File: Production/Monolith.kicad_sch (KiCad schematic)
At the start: 0 parts

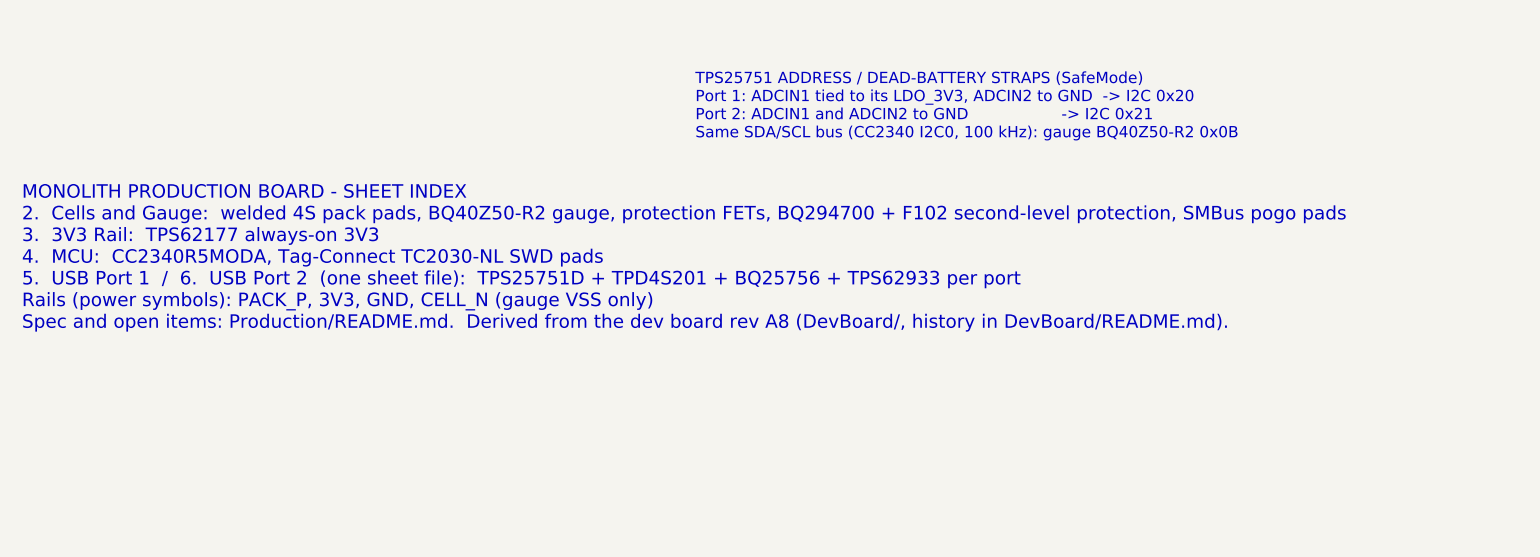
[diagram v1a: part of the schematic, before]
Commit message: Production schematic P0: U405/U505 TPD4S201 -> TPD2S300 (CC only)
CC keeps short-to-VBUS OVP and IEC ESD (TPS25751 CC pins are only +-1 kV
HBM); SBU half dropped with liquid detection, connector SBU pins no-connect.
VPWR/VM on LDO_3V3, VBIAS C451, FLT -> GPIO3. tools/tpd2s300.py. Netlist check
passes; ERC unchanged. Courtyard 1923 -> 1884 mm2.

Co-Authored-By: Claude Opus 5.5 <noreply@anthropic.com>
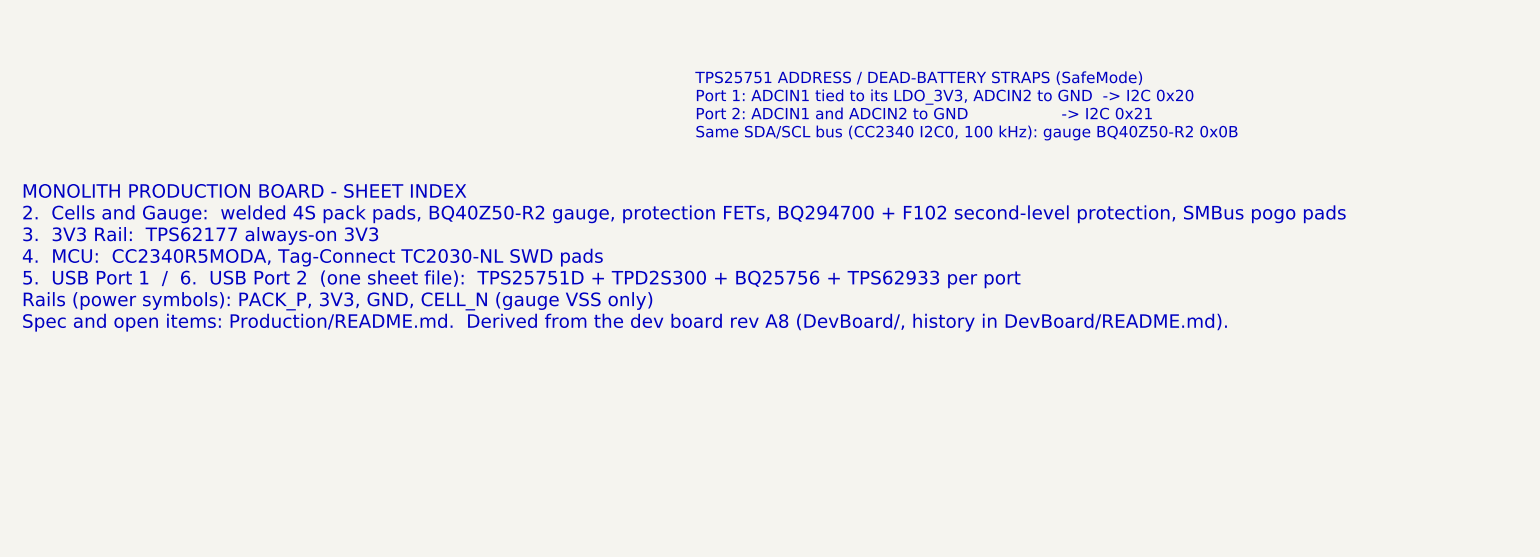
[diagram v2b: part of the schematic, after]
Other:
- note added: "MONOLITH PRODUCTION BOARD - SHEET INDEX 2. Cells and Gauge: welded 4S pack pads, BQ40Z50-R2 gauge, protection FETs, BQ294700 + F102 second-level protection, SMBus pogo pads 3. 3V3 Rail: TPS62177 always-on 3V3 4. MCU: CC2340R5MODA, Tag-Connect TC2030-NL SWD pads 5. USB Port 1 / 6. USB Port 2 (one sheet file): TPS25751D + TPD2S300 + BQ25756 + TPS62933 per port Rails (power symbols): PACK_P, 3V3, GN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"
- note removed: "MONOLITH PRODUCTION BOARD - SHEET INDEX 2. Cells and Gauge: welded 4S pack pads, BQ40Z50-R2 gauge, protection FETs, BQ294700 + F102 second-level protection, SMBus pogo pads 3. 3V3 Rail: TPS62177 always-on 3V3 4. MCU: CC2340R5MODA, Tag-Connect TC2030-NL SWD pads 5. USB Port 1 / 6. USB Port 2 (one sheet file): TPS25751D + TPD4S201 + BQ25756 + TPS62933 per port Rails (power symbols): PACK_P, 3V3, GN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"
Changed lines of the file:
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@@
 		(comment 3 "P0: dev board rev A8 stripped by Production/tools/make_production.py; not reviewed")
 	)
-	(text "MONOLITH PRODUCTION BOARD - SHEET INDEX\n2.  Cells and Gauge:  welded 4S pack pads, BQ40Z50-R2 gauge, protection FETs, BQ294700 + F102 second-level protection, SMBus pogo pads\n3.  3V3 Rail:  TPS62177 always-on 3V3\n4.  MCU:  CC2340R5MODA, Tag-Connect TC2030-NL SWD pads\n5.  USB Port 1  /  6.  USB Port 2  (one sheet file):  TPS25751D + TPD4S201 + BQ25756 + TPS62933 per port\nRails (power symbols): PACK_P, 3V3, GND, CELL_N (gauge VSS only)\nSpec and open items: Production/README.md.  Derived from the dev board rev A8 (DevBoard/, history in DevBoard/README.md)."
+	(text "MONOLITH PRODUCTION BOARD - SHEET INDEX\n2.  Cells and Gauge:  welded 4S pack pads, BQ40Z50-R2 gauge, protection FETs, BQ294700 + F102 second-level protection, SMBus pogo pads\n3.  3V3 Rail:  TPS62177 always-on 3V3\n4.  MCU:  CC2340R5MODA, Tag-Connect TC2030-NL SWD pads\n5.  USB Port 1  /  6.  USB Port 2  (one sheet file):  TPS25751D + TPD2S300 + BQ25756 + TPS62933 per port\nRails (power symbols): PACK_P, 3V3, GND, CELL_N (gauge VSS only)\nSpec and open items: Production/README.md.  Derived from the dev board rev A8 (DevBoard/, history in DevBoard/README.md)."
 		(exclude_from_sim no)
 		(at 30.48 205.74 0)

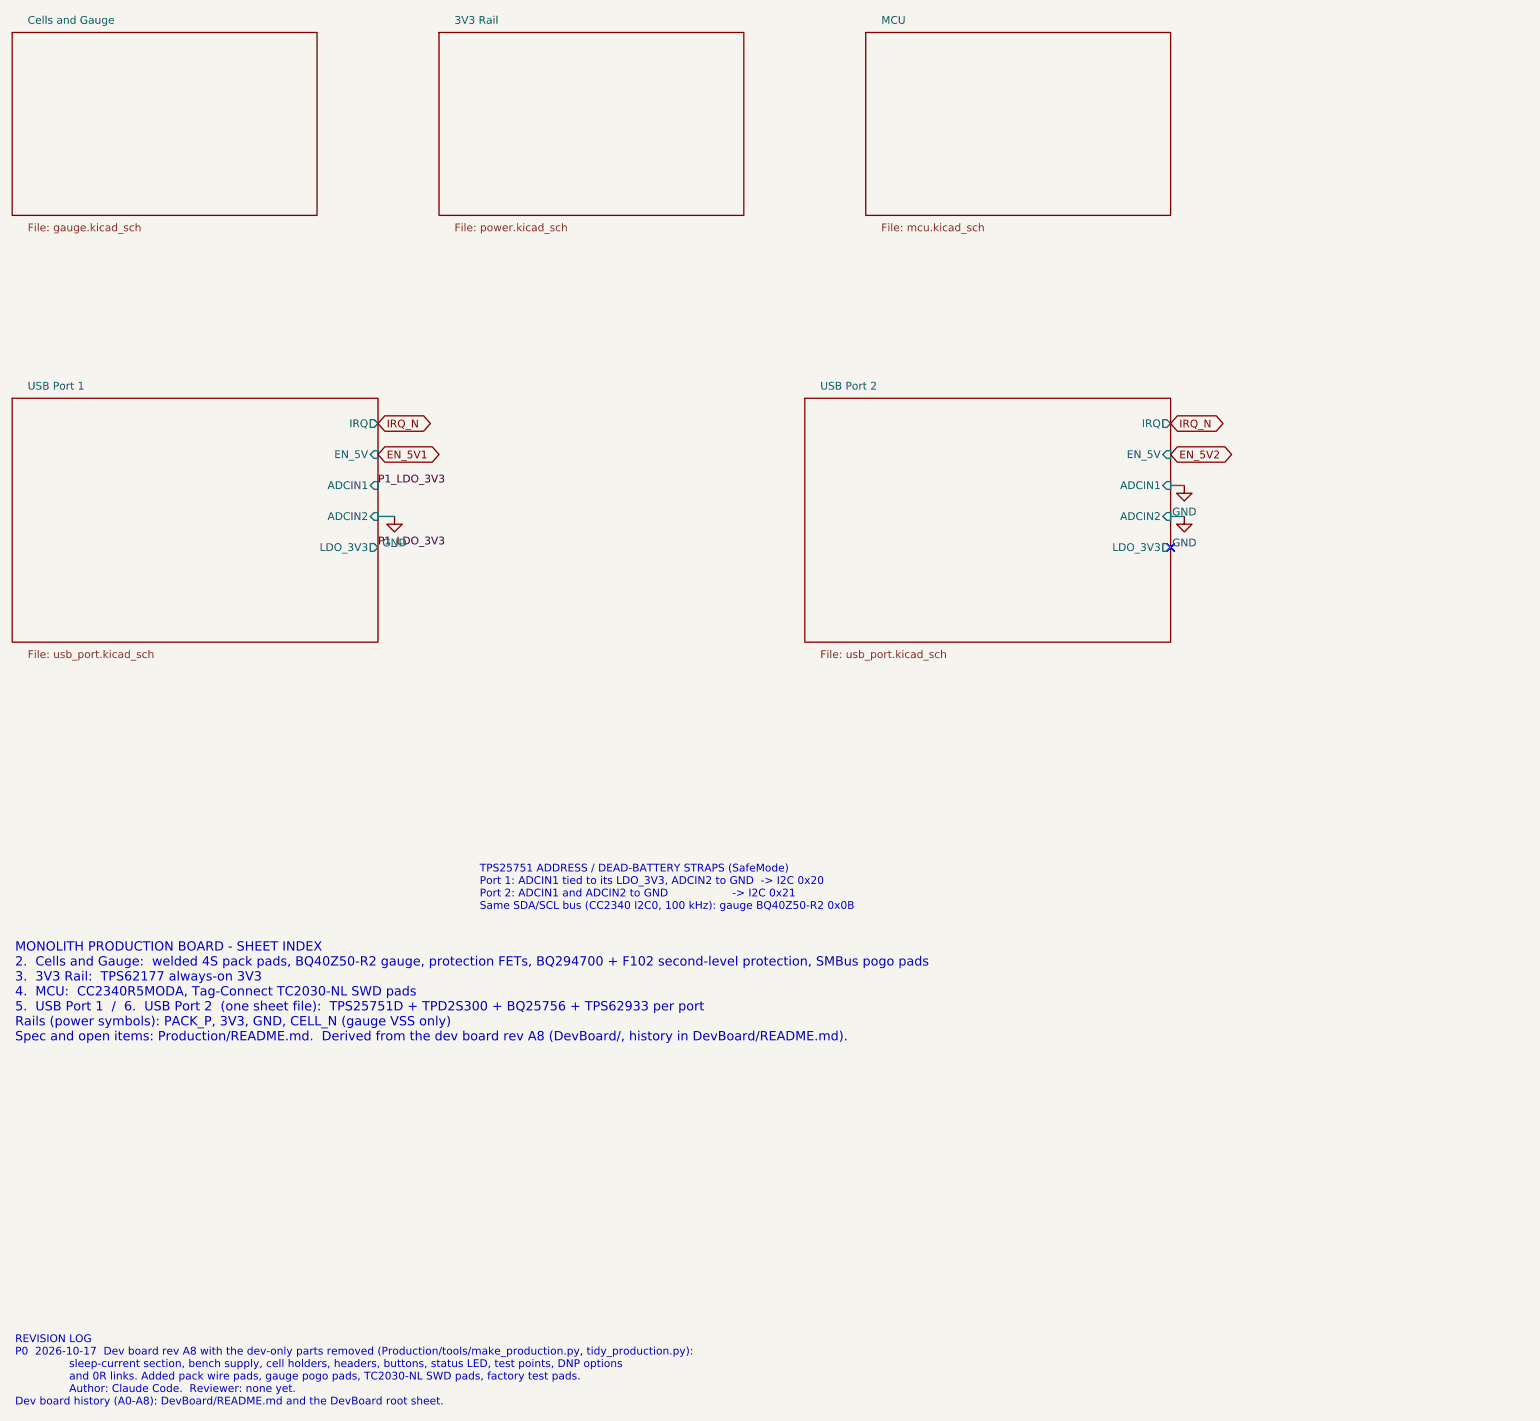
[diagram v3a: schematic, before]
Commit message: Production schematic P0: layout clean-up pass
New tools/layout_production.py (after make and tidy): block moves via
DevBoard/tools/move_region.py, then place_fields.py and check_overlaps.py.
Gauge: pack/NTC pads compacted, current sense and test/training pads moved up;
MCU: blocks regrouped, notes moved, J302 at 5.08 mm pin pitch; 3V3 Rail:
shared bulk and notes beside the rail; stale headings and index text fixed.
0 overlaps on all sheets; netlist check passes; ERC known warnings only.

Co-Authored-By: Claude Opus 5.5 <noreply@anthropic.com>
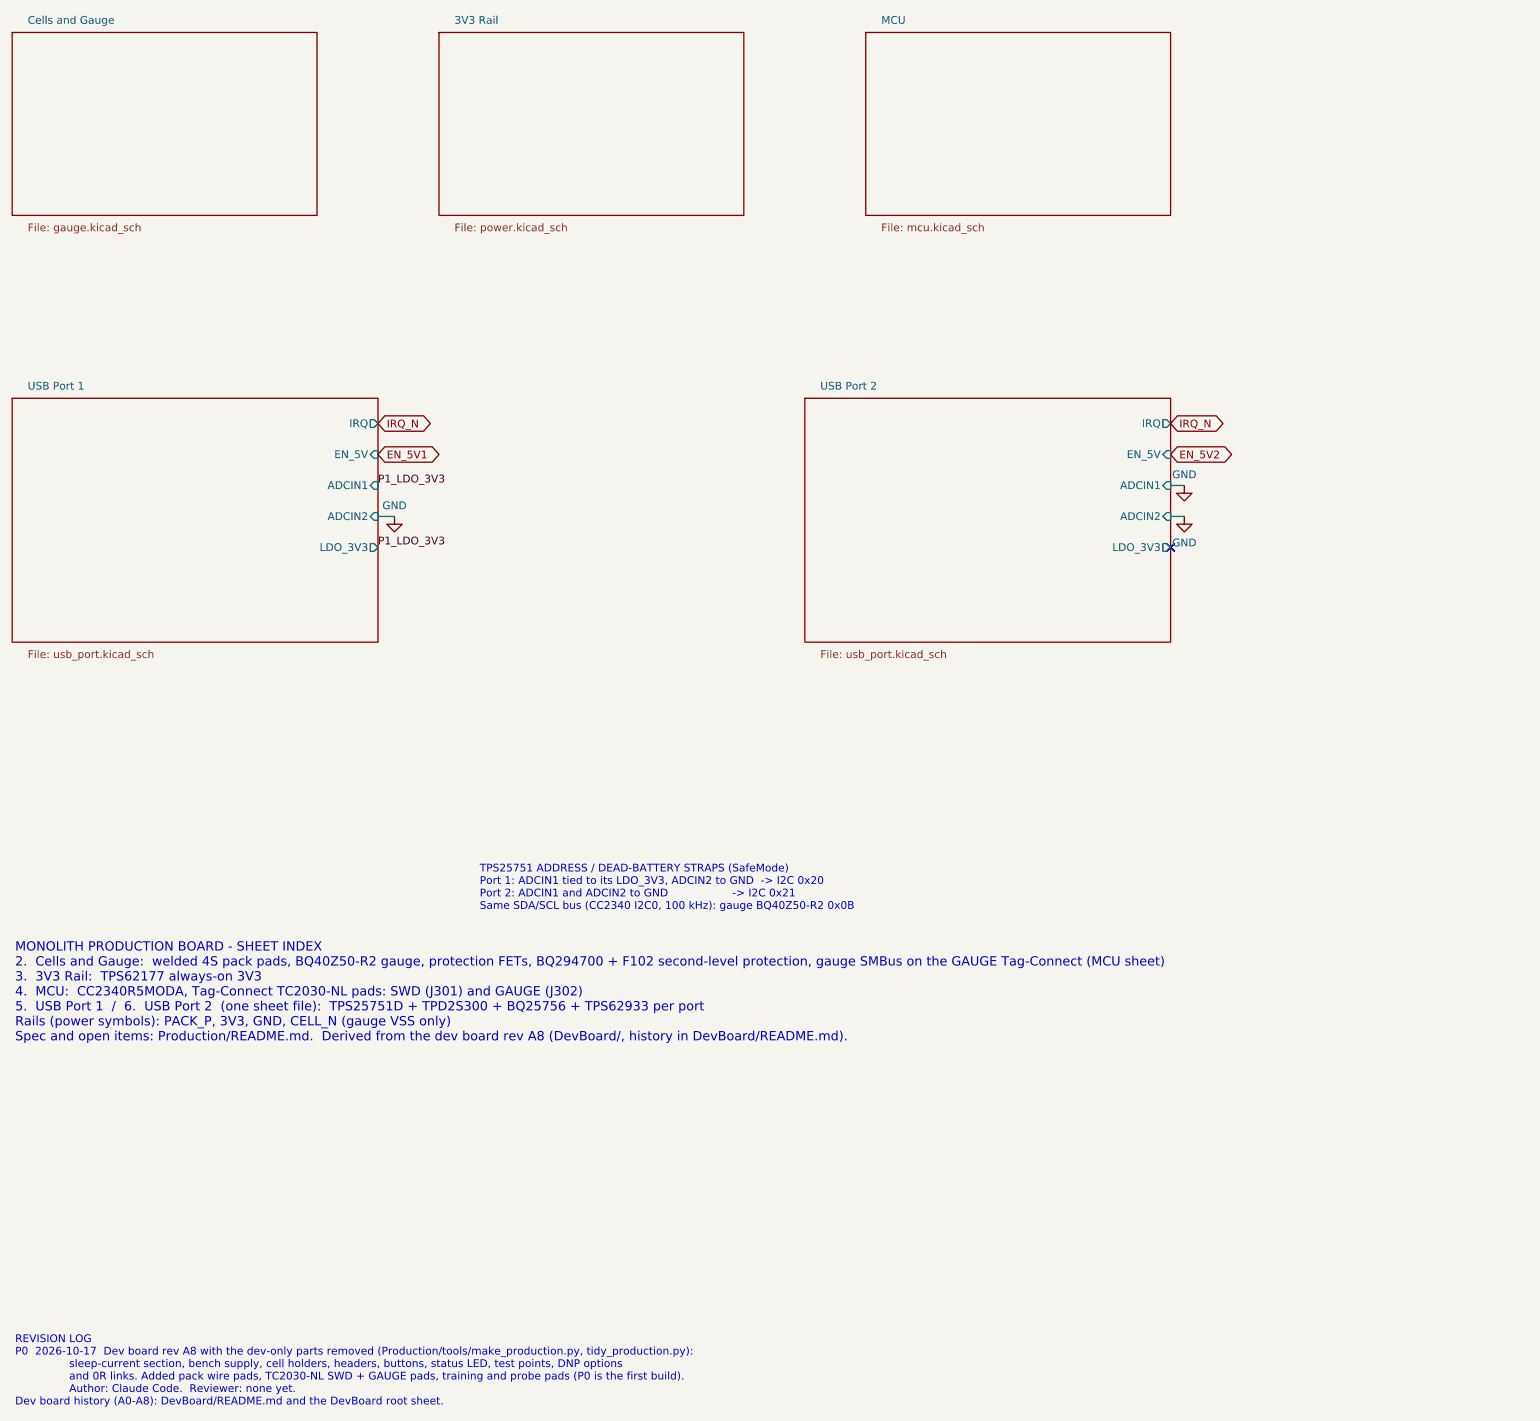
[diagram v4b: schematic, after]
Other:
- note added: "MONOLITH PRODUCTION BOARD - SHEET INDEX 2. Cells and Gauge: welded 4S pack pads, BQ40Z50-R2 gauge, protection FETs, BQ294700 + F102 second-level protection, gauge SMBus on the GAUGE Tag-Connect (MCU sheet) 3. 3V3 Rail: TPS62177 always-on 3V3 4. MCU: CC2340R5MODA, Tag-Connect TC2030-NL pads: SWD (J301) and GAUGE (J302) 5. USB Port 1 / 6. USB Port 2 (one sheet file): TPS25751D + TPD2S300 + BQ25756 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"
- note added: "REVISION LOG P0 2026-10-17 Dev board rev A8 with the dev-only parts removed (Production/tools/make_production.py, tidy_production.py): sleep-current section, bench supply, cell holders, headers, buttons, status LED, test points, DNP options and 0R links. Added pack wire pads, TC2030-NL SWD + GAUGE pads, training and probe pads (P0 is the first build). Author: Claude Code. Reviewer: none yet. Dev 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"
- note removed: "MONOLITH PRODUCTION BOARD - SHEET INDEX 2. Cells and Gauge: welded 4S pack pads, BQ40Z50-R2 gauge, protection FETs, BQ294700 + F102 second-level protection, SMBus pogo pads 3. 3V3 Rail: TPS62177 always-on 3V3 4. MCU: CC2340R5MODA, Tag-Connect TC2030-NL SWD pads 5. USB Port 1 / 6. USB Port 2 (one sheet file): TPS25751D + TPD2S300 + BQ25756 + TPS62933 per port Rails (power symbols): PACK_P, 3V3, GN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"
- note removed: "REVISION LOG P0 2026-10-17 Dev board rev A8 with the dev-only parts removed (Production/tools/make_production.py, tidy_production.py): sleep-current section, bench supply, cell holders, headers, buttons, status LED, test points, DNP options and 0R links. Added pack wire pads, gauge pogo pads, TC2030-NL SWD pads, factory test pads. Author: Claude Code. Reviewer: none yet. Dev board history (A0-A8)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"
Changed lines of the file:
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@@
 		(comment 3 "P0: dev board rev A8 stripped by Production/tools/make_production.py; not reviewed")
 	)
-	(text "MONOLITH PRODUCTION BOARD - SHEET INDEX\n2.  Cells and Gauge:  welded 4S pack pads, BQ40Z50-R2 gauge, protection FETs, BQ294700 + F102 second-level protection, SMBus pogo pads\n3.  3V3 Rail:  TPS62177 always-on 3V3\n4.  MCU:  CC2340R5MODA, Tag-Connect TC2030-NL SWD pads\n5.  USB Port 1  /  6.  USB Port 2  (one sheet file):  TPS25751D + TPD2S300 + BQ25756 + TPS62933 per port\nRails (power symbols): PACK_P, 3V3, GND, CELL_N (gauge VSS only)\nSpec and open items: Production/README.md.  Derived from the dev board rev A8 (DevBoard/, history in DevBoard/README.md)."
+	(text "MONOLITH PRODUCTION BOARD - SHEET INDEX\n2.  Cells and Gauge:  welded 4S pack pads, BQ40Z50-R2 gauge, protection FETs, BQ294700 + F102 second-level protection, gauge SMBus on the GAUGE Tag-Connect (MCU sheet)\n3.  3V3 Rail:  TPS62177 always-on 3V3\n4.  MCU:  CC2340R5MODA, Tag-Connect TC2030-NL pads: SWD (J301) and GAUGE (J302)\n5.  USB Port 1  /  6.  USB Port 2  (one sheet file):  TPS25751D + TPD2S300 + BQ25756 + TPS62933 per port\nRails (power symbols): PACK_P, 3V3, GND, CELL_N (gauge VSS only)\nSpec and open items: Production/README.md.  Derived from the dev board rev A8 (DevBoard/, history in DevBoard/README.md)."
 		(exclude_from_sim no)
 		(at 30.48 205.74 0)
@@
 		)
 	)
-	(text "REVISION LOG\nP0  2026-10-17  Dev board rev A8 with the dev-only parts removed (Production/tools/make_production.py, tidy_production.py):\n                sleep-current section, bench supply, cell holders, headers, buttons, status LED, test points, DNP options\n                and 0R links. Added pack wire pads, gauge pogo pads, TC2030-NL SWD pads, factory test pads.\n                Author: Claude Code.  Reviewer: none yet.\nDev board history (A0-A8): DevBoard/README.md and the DevBoard root sheet."
+	(text "REVISION LOG\nP0  2026-10-17  Dev board rev A8 with the dev-only parts removed (Production/tools/make_production.py, tidy_production.py):\n                sleep-current section, bench supply, cell holders, headers, buttons, status LED, test points, DNP options\n                and 0R links. Added pack wire pads, TC2030-NL SWD + GAUGE pads, training and probe pads (P0 is the first build).\n                Author: Claude Code.  Reviewer: none yet.\nDev board history (A0-A8): DevBoard/README.md and the DevBoard root sheet."
 		(exclude_from_sim no)
 		(at 30.48 265.43 0)
@@
 		)
 		(property "Value" "GND"
-			(at 222.25 123.7 0)
+			(at 222.25 123.70 0)
 			(show_name no)
 			(do_not_autoplace no)
@@
 		)
 		(property "Value" "GND"
-			(at 222.25 118.62 0)
+			(at 222.25 112.52 0)
 			(show_name no)
 			(do_not_autoplace no)
@@
 		)
 		(property "Value" "GND"
-			(at 92.71 123.7 0)
-			(show_name no)
-			(do_not_autoplace no)
+			(at 92.71 117.60 0)
+			(show_name no)
+			(do_not_autoplace no)
